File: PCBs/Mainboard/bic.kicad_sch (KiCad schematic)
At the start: 19 parts, among them IC4 MIC5303-1.8YMT-TR, J2 TERMISTOR, J3 BAT_CONN, U2 BQ25628ERYKR, U3 TPS62291DRVR

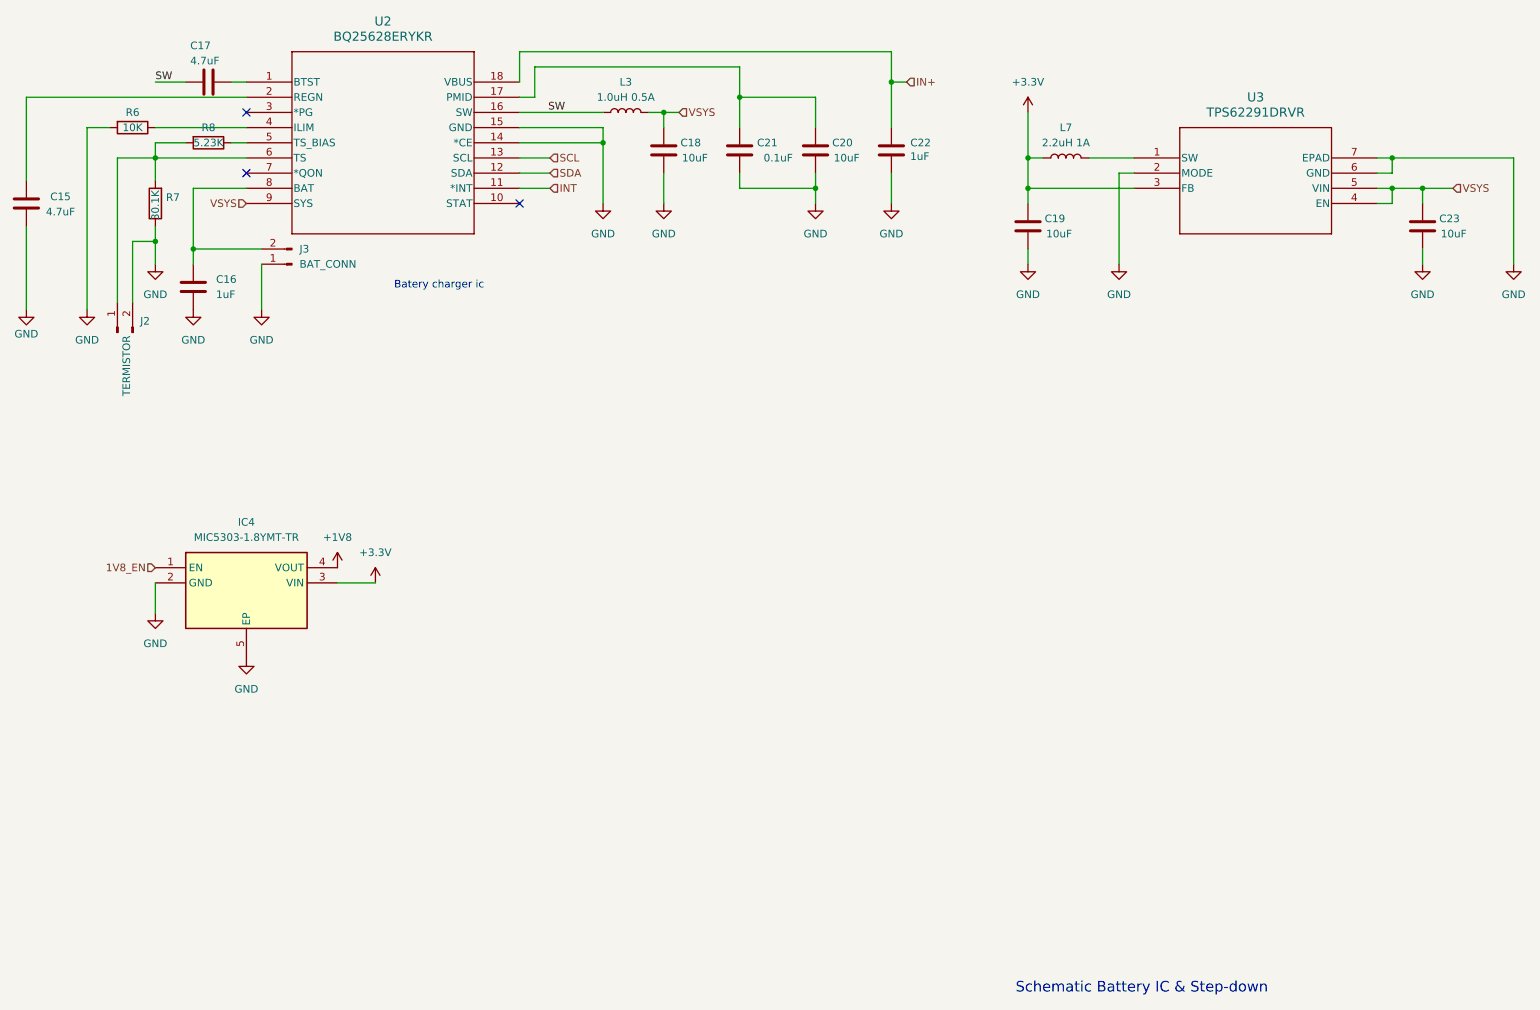
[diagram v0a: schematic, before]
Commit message: Add progress report for 31.1.2025 Update relevant source files
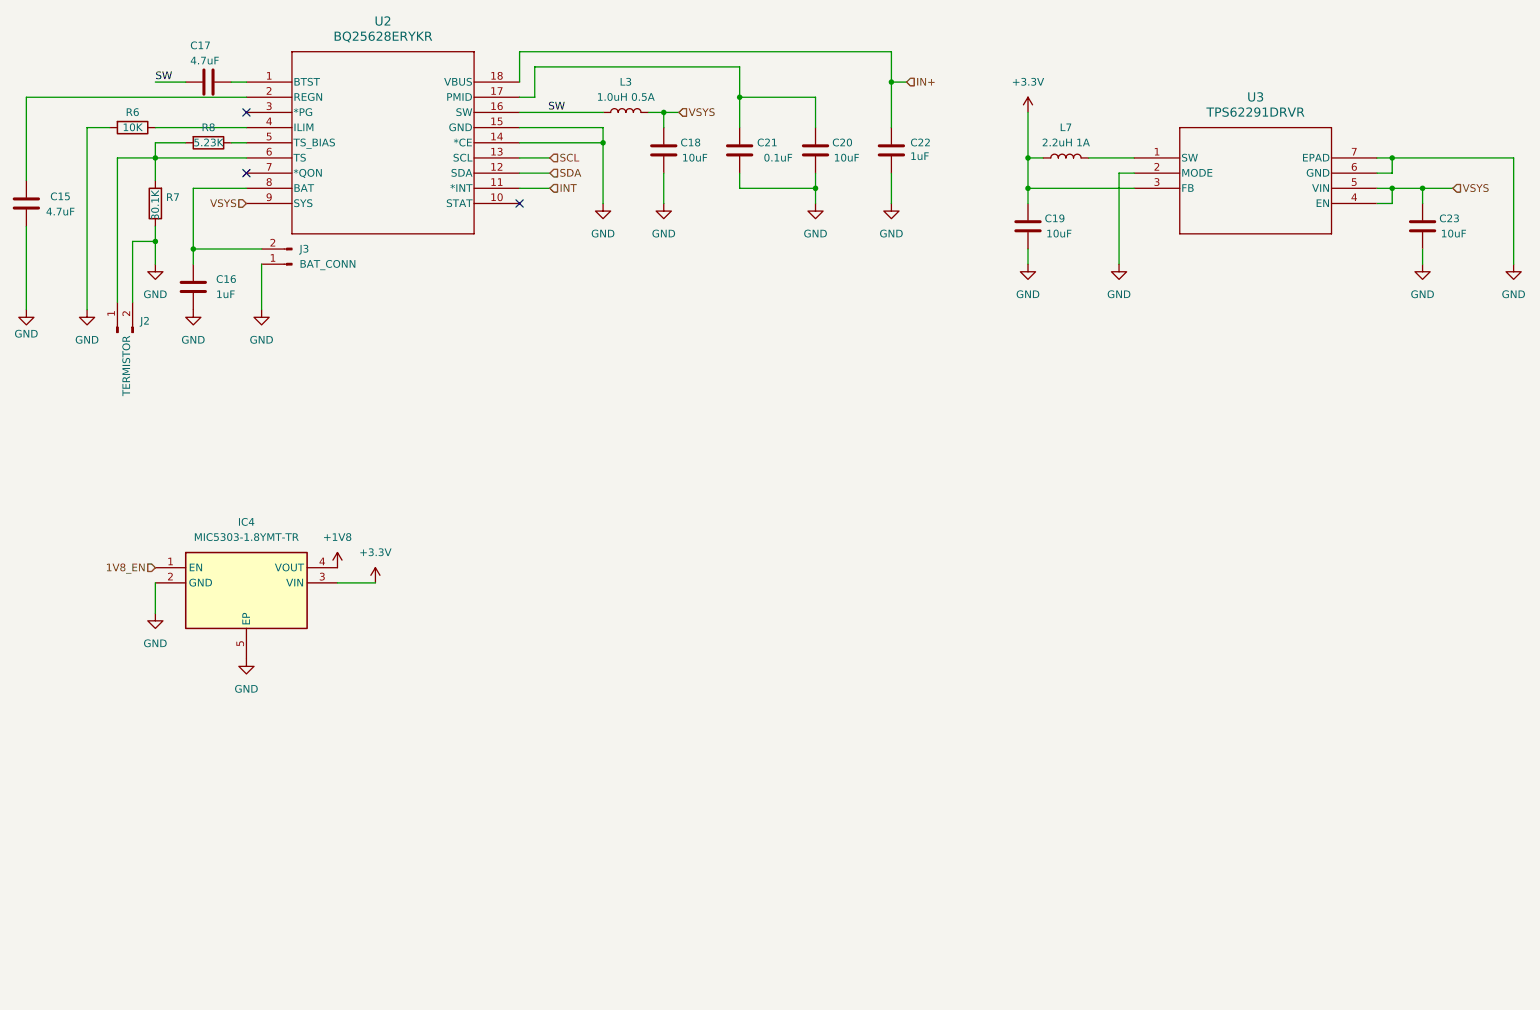
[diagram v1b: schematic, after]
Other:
- note removed: "Batery charger ic"
- note removed: "Schematic Battery IC & Step-down"
- title: (none) -> Battery IC & Step-down
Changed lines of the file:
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@@
 	(generator_version "8.0")
 	(paper "A4")
+	(title_block
+		(title "Battery IC & Step-down")
+	)
 	(junction
 		(at 45.72 64.77)
@@
 		)
 	)
-	(text "Batery charger ic"
-		(exclude_from_sim no)
-		(at 93.218 72.136 0)
-		(effects
-			(font
-				(size 1.27 1.27)
-			)
-		)
-	)
-	(text "Schematic Battery IC & Step-down"
-		(exclude_from_sim no)
-		(at 210.82 189.738 0)
-		(effects
-			(font
-				(size 1.778 1.778)
-			)
-		)
-	)
 	(label "SW"
 		(at 45.72 38.1 0)
-		(fields_autoplaced yes)
 		(effects
 			(font
@@
 	(label "SW"
 		(at 114.3 43.18 180)
-		(fields_autoplaced yes)
 		(effects
 			(font
@@
 		(shape input)
 		(at 133.35 43.18 0)
-		(fields_autoplaced yes)
 		(effects
 			(font
@@
 		(shape input)
 		(at 171.45 38.1 0)
-		(fields_autoplaced yes)
 		(effects
 			(font
@@
 		(shape input)
 		(at 45.72 119.38 180)
-		(fields_autoplaced yes)
 		(effects
 			(font
@@
 		(shape input)
 		(at 111.76 50.8 0)
-		(fields_autoplaced yes)
 		(effects
 			(font
@@
 		(shape input)
 		(at 60.96 58.42 180)
-		(fields_autoplaced yes)
 		(effects
 			(font
@@
 		(shape input)
 		(at 262.89 55.88 0)
-		(fields_autoplaced yes)
 		(effects
 			(font
@@
 		(shape input)
 		(at 111.76 55.88 0)
-		(fields_autoplaced yes)
 		(effects
 			(font
@@
 		(shape input)
 		(at 111.76 53.34 0)
-		(fields_autoplaced yes)
-		(effects
-			(font
+		(effects
+			(font
